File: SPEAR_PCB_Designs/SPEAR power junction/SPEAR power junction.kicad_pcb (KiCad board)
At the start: 2 copper layers, 77 x 46.5 mm, 7 parts, among them J1 XT30PW-M, J2 XT30PW-M, J3 XT30PW-M, J5 XT90PW-M

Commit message: updates to design
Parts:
- moved J1 14.5 mm to (194.5, 106.5), turned to -90 degrees
- moved J3 14.5 mm to (194.5, 75.5), turned to -90 degrees
- moved J2 14.5 mm to (194.5, 91.0), turned to -90 degrees
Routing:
- net Net-(F6-Pad2_1): track 24.0 -> 17.7 mm
- net Net-(F5-Pad2_1): track 23.3 -> 17.2 mm
- net Net-(F4-Pad2_1): track 23.2 -> 17.2 mm

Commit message: Updated Power junction design and fabrication folder
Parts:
- added F1: 3557-15, 3557-15:FUSE_3557-15, F.Cu at (157.2, 81.7)
- added J4: SM02B-GHS-TB, SM02B-GHS-TB:CONN_SM02B-GHS_JST, F.Cu at (135.9, 72.5)
- moved J5 11.4 mm to (149.0, 101.5)
- moved F4 8.29 mm to (172.3, 106.2)
- moved F6 8.27 mm to (172.3, 73.7)
- moved F5 8.26 mm to (172.3, 90.0)
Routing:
- net GND: track 0.00 -> 48.8 mm, vias 0 -> 1
- net Net-(F1-Pad2_1): track 0.00 -> 15.1 mm
- net Net-(F6-Pad2_1): track 17.7 -> 9.31 mm
- net Net-(F5-Pad2_1): track 17.2 -> 8.98 mm
- net Net-(F4-Pad2_1): track 17.2 -> 9.11 mm
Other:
- board size 77 x 46.5 mm -> 65 x 51.5 mm
- board text added: "+"
- board text added: "-"
- board text added: "15A"
- board text added: "1A"
- board text added: "Joelle Adedun"
- board text added: "PO1"
- board text added: "PO2"
- board text added: "PO3"
- board text added: "Power Junction Version 1"
- board text added: "Power in"
- board text added: "SPEAR"

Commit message: Update SPEAR power junction.kicad_pcb
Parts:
- added REF**: MountingHole_3.2mm_M3, MountingHole:MountingHole_3.2mm_M3, F.Cu at (137.0, 82.0)
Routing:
- net GND: track 48.8 -> 1.80 mm
- net Net-(F4-Pad2_1): track 9.11 -> 0.00 mm
- net Net-(F1-Pad2_1): track 15.1 -> 18.5 mm
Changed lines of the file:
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@@
 		)
 		(property "Value" "SM02B-GHS-TB"
-			(at 9.970549 0.1759 -90)
+			(at 7.470549 -7.124099 -90)
 			(unlocked yes)
 			(layer "F.Fab")
@@
 		)
 	)
+	(footprint "MountingHole:MountingHole_3.2mm_M3"
+		(layer "F.Cu")
+		(at 137 82)
+		(descr "Mounting Hole 3.2mm, no annular, M3")
+		(tags "mounting hole 3.2mm no annular m3")
+		(property "Reference" "REF**"
+			(at 0 -4.2 0)
+			(layer "F.SilkS")
+			(effects
+				(font
+					(size 1 1)
+					(thickness 0.15)
+				)
+			)
+		)
+		(property "Value" "MountingHole_3.2mm_M3"
+			(at 6 5.5 0)
+			(layer "F.Fab")
+			(effects
+				(font
+					(size 1 1)
+					(thickness 0.15)
+				)
+			)
+		)
+		(property "Footprint" ""
+			(at 0 0 0)
+			(unlocked yes)
+			(layer "F.Fab")
+			(hide yes)
+			(effects
+				(font
+					(size 1.27 1.27)
+					(thickness 0.15)
+				)
+			)
+		)
+		(property "Datasheet" ""
+			(at 0 0 0)
+			(unlocked yes)
+			(layer "F.Fab")
+			(hide yes)
+			(effects
+				(font
+					(size 1.27 1.27)
+					(thickness 0.15)
+				)
+			)
+		)
+		(property "Description" ""
+			(at 0 0 0)
+			(unlocked yes)
+			(layer "F.Fab")
+			(hide yes)
+			(effects
+				(font
+					(size 1.27 1.27)
+					(thickness 0.15)
+				)
+			)
+		)
+		(attr exclude_from_pos_files exclude_from_bom)
+		(fp_circle
+			(center 0 0)
+			(end 3.2 0)
+			(stroke
+				(width 0.15)
+				(type solid)
+			)
+			(fill none)
+			(layer "Cmts.User")
+		)
+		(fp_circle
+			(center 0 0)
+			(end 3.45 0)
+			(stroke
+				(width 0.05)
+				(type solid)
+			)
+			(fill none)
+			(layer "F.CrtYd")
+		)
+		(fp_text user "${REFERENCE}"
+			(at 0 0 0)
+			(layer "F.Fab")
+			(effects
+				(font
+					(size 1 1)
+					(thickness 0.15)
+				)
+			)
+		)
+		(pad "" np_thru_hole circle
+			(at 0 0)
+			(size 3.2 3.2)
+			(drill 3.2)
+			(layers "*.Cu" "*.Mask")
+		)
+	)
 	(footprint "XT30PW-M:AMASS_XT30PW-M"
 		(layer "F.Cu")
@@
 	)
 	(gr_text "Joelle Adedun"
-		(at 142 70 0)
+		(at 156.5 69.5 -0)
 		(layer "B.SilkS")
 		(effects
@@
 				(bold yes)
 			)
-			(justify left bottom)
+			(justify left bottom mirror)
 		)
 	)
 	(gr_text "SPEAR"
-		(at 138.5 86 0)
+		(at 155 74 -0)
 		(layer "B.SilkS")
 		(effects
@@
 				(bold yes)
 			)
-			(justify left bottom)
+			(justify left bottom mirror)
 		)
 	)
@@
 	)
 	(segment
-		(start 179 104.5)
-		(end 179 107.9)
-		(width 6.29)
-		(layer "F.Cu")
-		(net 2)
-	)
-	(segment
-		(start 179.5 104)
-		(end 179 104.5)
-		(width 6.29)
-		(layer "F.Cu")
-		(net 2)
-	)
-	(segment
-		(start 184.5 104)
-		(end 179.5 104)
-		(width 6.29)
-		(layer "F.Cu")
-		(net 2)
-	)
-	(segment
 		(start 179 88.3)
 		(end 179 91.7)
@@
 	)
 	(segment
-		(start 150.404451 71.904451)
+		(start 140 71.904451)
 		(end 138.200001 71.904451)
 		(width 0.2)
@@
 		(net 5)
 	)
-	(segment
-		(start 150.404451 71.904451)
-		(end 155 76.5)
-		(width 0.2)
-		(layer "F.Cu")
-		(net 5)
-	)
 	(via
-		(at 155 76.5)
+		(at 140 71.904451)
 		(size 0.6)
 		(drill 0.3)
@@
 	)
 	(segment
-		(start 156.5 78)
-		(end 184.5 78)
+		(start 143.654451 73.154451)
+		(end 150.5 80)
 		(width 0.2)
-		(layer "B.Cu")
-		(net 5)
+		(layer "F.Cu")
+		(net 14)
 	)
 	(segment
-		(start 155 76.5)
-		(end 156.5 78)
+		(start 138.200001 73.154451)
+		(end 143.654451 73.154451)
 		(width 0.2)
-		(layer "B.Cu")
-		(net 5)
-	)
-	(segment
-		(start 150.5 80)
-		(end 145.04555 80)
-		(width 6.29)
 		(layer "F.Cu")
 		(net 14)
@@
 		(net 14)
 	)
-	(segment
-		(start 145.04555 80)
-		(end 140.625201 75.579651)
-		(width 6.29)
+	(zone
+		(net 1)
+		(net_name "Power")
 		(layer "F.Cu")
-		(net 14)
+		(hatch edge 0.5)
+		(priority 2)
+		(connect_pads
+			(clearance 0.5)
+		)
+		(min_thickness 0.25)
+		(filled_areas_thickness no)
+		(fill yes
+			(thermal_gap 0.5)
+			(thermal_bridge_width 0.5)
+		)
+		(polygon
+			(pts
+				(xy 177 110.5) (xy 182.5 110.5) (xy 182.5 106.5) (xy 187 106.5) (xy 187 101) (xy 177 101) (xy 177 104)
+			)
+		)
 	)
 	(zone

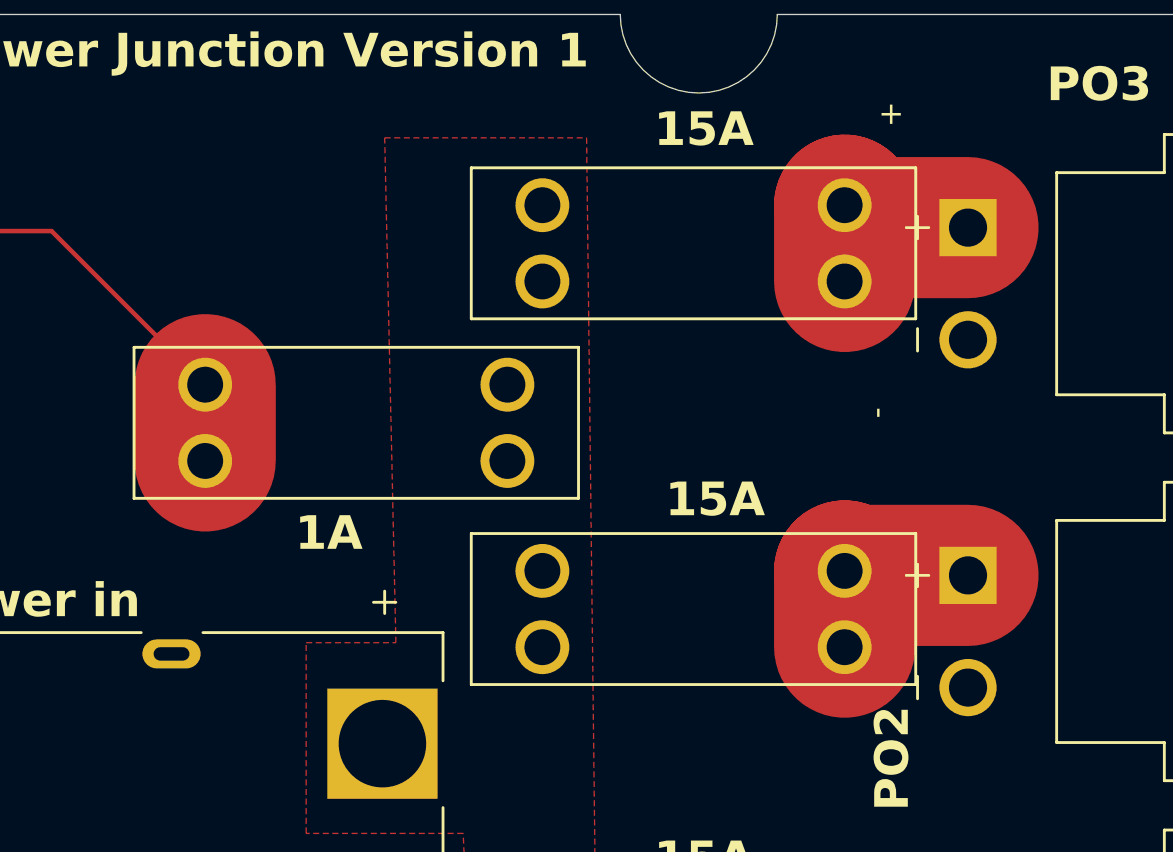
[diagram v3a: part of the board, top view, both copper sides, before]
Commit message: updates to pcb power junction design
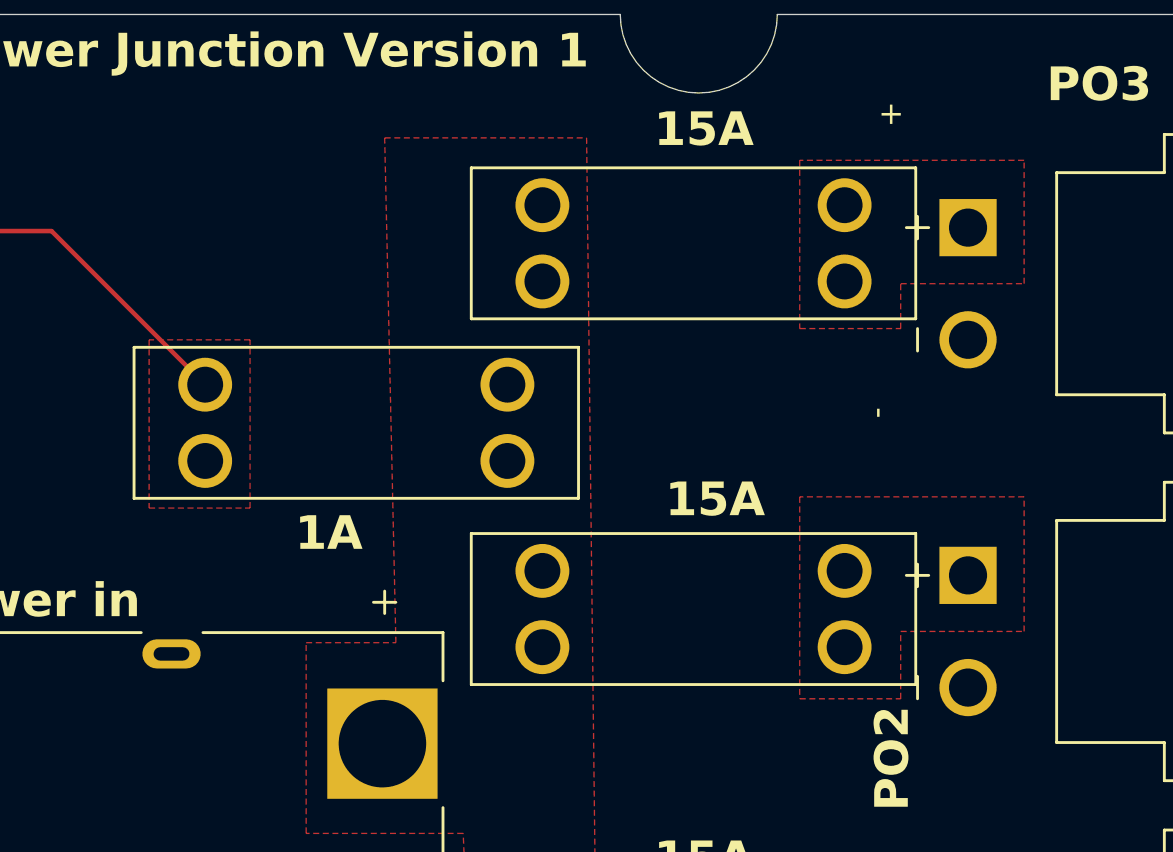
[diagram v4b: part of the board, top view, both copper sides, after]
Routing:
- net Net-(F6-Pad2_1): track 9.31 -> 0.00 mm
- net Net-(F5-Pad2_1): track 8.98 -> 0.00 mm
- net Net-(F1-Pad2_1): track 18.5 -> 15.1 mm
- added copper zone on F.Cu, net Net-(F1-Pad2_1)
- added copper zone on F.Cu, net Net-(F4-Pad2_1)
- added copper zone on F.Cu, net Net-(F5-Pad2_1)
- added copper zone on F.Cu, net Net-(F6-Pad2_1)
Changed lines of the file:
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@@
 			(drillshape 0)
 			(scaleselection 1)
-			(outputdirectory "C:/Users/jaded/OneDrive/Documents/SPEAR/Fabrication/")
+			(outputdirectory "Fabrication/")
 		)
 	)
@@
 			(solder_mask_margin 0.102)
 		)
-		(model "C:/Users/jaded/Downloads/XT30PW-M/XT30PW-M.step"
+		(model "${SPEAR_PCB_2026_DIR}/SPEAR_3D_Models/SPEAR_Power_Junction/XT30PW-M.step"
 			(offset
 				(xyz 0 0 0)
@@
 			)
 			(rotate
-				(xyz 0 0 0)
+				(xyz -90 0 0)
 			)
 		)
@@
 			(solder_mask_margin 0.102)
 		)
-		(model "C:/Users/jaded/Downloads/3557-15/3557-15.step"
+		(model "${SPEAR_PCB_2026_DIR}/SPEAR_3D_Models/SPEAR_Power_Junction/3557-15.step"
 			(offset
-				(xyz 0 0 0)
+				(xyz 0 0 4)
 			)
 			(scale
@@
 			)
 			(rotate
-				(xyz 0 0 0)
+				(xyz -90 0 0)
 			)
 		)
@@
 			(solder_mask_margin 0.102)
 		)
-		(model "C:/Users/jaded/Downloads/3557-15/3557-15.step"
+		(model "${SPEAR_PCB_2026_DIR}/SPEAR_3D_Models/SPEAR_Power_Junction/3557-15.step"
 			(offset
-				(xyz 0 0 0)
+				(xyz 0 0 4)
 			)
 			(scale
@@
 			)
 			(rotate
-				(xyz 0 0 0)
+				(xyz -90 0 0)
 			)
 		)
@@
 			(solder_mask_margin 0.102)
 		)
-		(model "C:/Users/jaded/Downloads/XT30PW-M/XT30PW-M.step"
+		(model "${SPEAR_PCB_2026_DIR}/SPEAR_3D_Models/SPEAR_Power_Junction/XT30PW-M.step"
 			(offset
 				(xyz 0 0 0)
@@
 			)
 			(rotate
-				(xyz 0 0 0)
+				(xyz -90 0 0)
 			)
 		)
@@
 			(solder_mask_margin 0.102)
 		)
-		(model "C:/Users/jaded/Downloads/3557-15/3557-15.step"
+		(model "${SPEAR_PCB_2026_DIR}/SPEAR_3D_Models/SPEAR_Power_Junction/3557-15.step"
 			(offset
-				(xyz 0 0 0)
+				(xyz 0 0 4)
 			)
 			(scale
@@
 			)
 			(rotate
-				(xyz 0 0 0)
+				(xyz -90 0 0)
 			)
 		)
@@
 			(layers "F.Cu" "F.Paste" "F.Mask")
 		)
-		(model "C:/Users/jaded/Downloads/ul_SM02B-GHS-TB/KiCADv6/SM02B-GHS-TB -LF--SN---3DModel-STEP-56544.STEP"
+		(model "${SPEAR_PCB_2026_DIR}/SPEAR_3D_Models/SPEAR_Power_Junction/SM02B-GHS-TB -LF--SN---3DModel-STEP-56544.STEP"
 			(offset
 				(xyz 0 0 0)
@@
 			(solder_mask_margin 0.102)
 		)
-		(model "C:/Users/jaded/Downloads/3557-15/3557-15.step"
+		(model "${SPEAR_PCB_2026_DIR}/SPEAR_3D_Models/SPEAR_Power_Junction/3557-15.step"
 			(offset
-				(xyz 0 0 0)
+				(xyz 0 0 4)
 			)
 			(scale
@@
 			)
 			(rotate
-				(xyz 0 0 0)
+				(xyz -90 0 0)
 			)
 		)
@@
 			(solder_mask_margin 0.102)
 		)
-		(model "C:/Users/jaded/Downloads/XT90PW-M (3)/XT90PW-M.step"
+		(model "${SPEAR_PCB_2026_DIR}/SPEAR_3D_Models/SPEAR_Power_Junction/XT90PW-M.step"
 			(offset
 				(xyz 0 0 0)
@@
 			)
 			(rotate
-				(xyz 0 0 0)
+				(xyz -90 0 0)
 			)
 		)
@@
 			(solder_mask_margin 0.102)
 		)
-		(model "C:/Users/jaded/Downloads/XT30PW-M/XT30PW-M.step"
+		(model "${SPEAR_PCB_2026_DIR}/SPEAR_3D_Models/SPEAR_Power_Junction/XT30PW-M.step"
 			(offset
 				(xyz 0 0 0)
@@
 			)
 			(rotate
-				(xyz 0 0 0)
+				(xyz -90 0 0)
 			)
 		)
@@
 	)
 	(segment
-		(start 179 88.3)
-		(end 179 91.7)
-		(width 6.29)
-		(layer "F.Cu")
-		(net 3)
-	)
-	(segment
-		(start 184.5 88.5)
-		(end 179.2 88.5)
-		(width 6.29)
-		(layer "F.Cu")
-		(net 3)
-	)
-	(segment
-		(start 179.2 88.5)
-		(end 179 88.3)
-		(width 6.29)
-		(layer "F.Cu")
-		(net 3)
-	)
-	(segment
-		(start 184.5 73)
-		(end 180 73)
-		(width 6.29)
-		(layer "F.Cu")
-		(net 4)
-	)
-	(segment
-		(start 180 73)
-		(end 179 72)
-		(width 6.29)
-		(layer "F.Cu")
-		(net 4)
-	)
-	(segment
-		(start 179 75.4)
-		(end 179 72)
-		(width 6.29)
-		(layer "F.Cu")
-		(net 4)
-	)
-	(segment
 		(start 140 71.904451)
 		(end 138.200001 71.904451)
@@
 		(net 14)
 	)
-	(segment
-		(start 150.5 83.4)
-		(end 150.5 80)
-		(width 6.29)
+	(zone
+		(net 4)
+		(net_name "Net-(F6-Pad2_1)")
 		(layer "F.Cu")
+		(hatch edge 0.5)
+		(priority 4)
+		(connect_pads
+			(clearance 0.5)
+		)
+		(min_thickness 0.25)
+		(filled_areas_thickness no)
+		(fill yes
+			(thermal_gap 0.5)
+			(thermal_bridge_width 0.5)
+		)
+		(polygon
+			(pts
+				(xy 177 70) (xy 177 77.5) (xy 181.5 77.5) (xy 181.5 75.5) (xy 187 75.5) (xy 187 70)
+			)
+		)
+	)
+	(zone
 		(net 14)
+		(net_name "Net-(F1-Pad2_1)")
+		(layer "F.Cu")
+		(hatch edge 0.5)
+		(priority 5)
+		(connect_pads
+			(clearance 0.5)
+		)
+		(min_thickness 0.25)
+		(filled_areas_thickness no)
+		(fill yes
+			(thermal_gap 0.5)
+			(thermal_bridge_width 0.5)
+		)
+		(polygon
+			(pts
+				(xy 148 78) (xy 148 85.5) (xy 152.5 85.5) (xy 152.5 78)
+			)
+		)
 	)
 	(zone
-		(net 1)
-		(net_name "Power")
+		(net 2)
+		(net_name "Net-(F4-Pad2_1)")
 		(layer "F.Cu")
 		(hatch edge 0.5)
@@
 			)
 		)
+	)
+	(zone
+		(net 3)
+		(net_name "Net-(F5-Pad2_1)")
+		(layer "F.Cu")
+		(hatch edge 0.5)
+		(priority 3)
+		(connect_pads
+			(clearance 0.5)
+		)
+		(min_thickness 0.25)
+		(filled_areas_thickness no)
+		(fill yes
+			(thermal_gap 0.5)
+			(thermal_bridge_width 0.5)
+		)
+		(polygon
+			(pts
+				(xy 177 85) (xy 177 94) (xy 181.5 94) (xy 181.5 91) (xy 187 91) (xy 187 85)
+			)
+		)
